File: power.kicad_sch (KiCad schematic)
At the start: 10 parts, among them J5 JST_PH_B2B, U2 MCP73831-2-OT, U3 AP1117-33

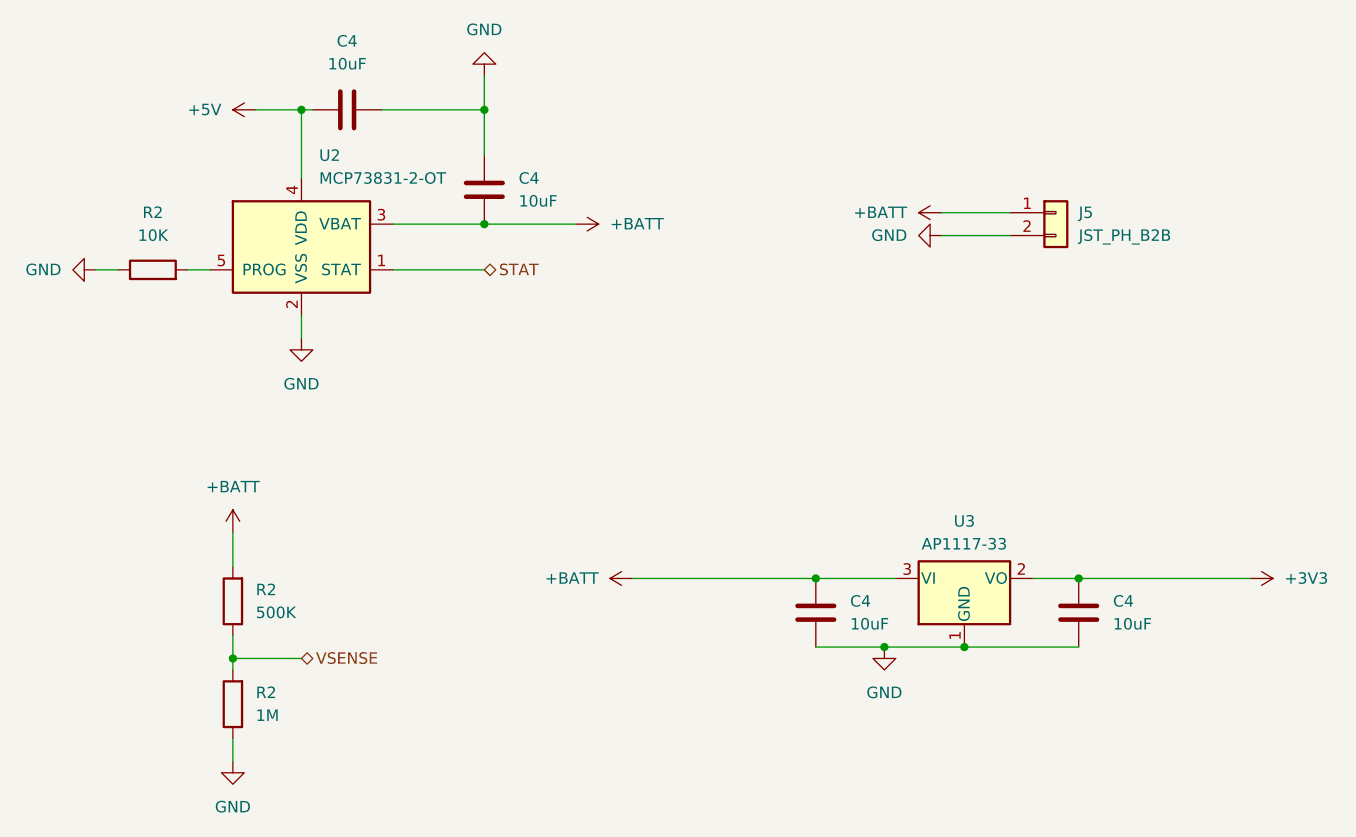
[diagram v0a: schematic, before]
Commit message: Removed audio, more routing
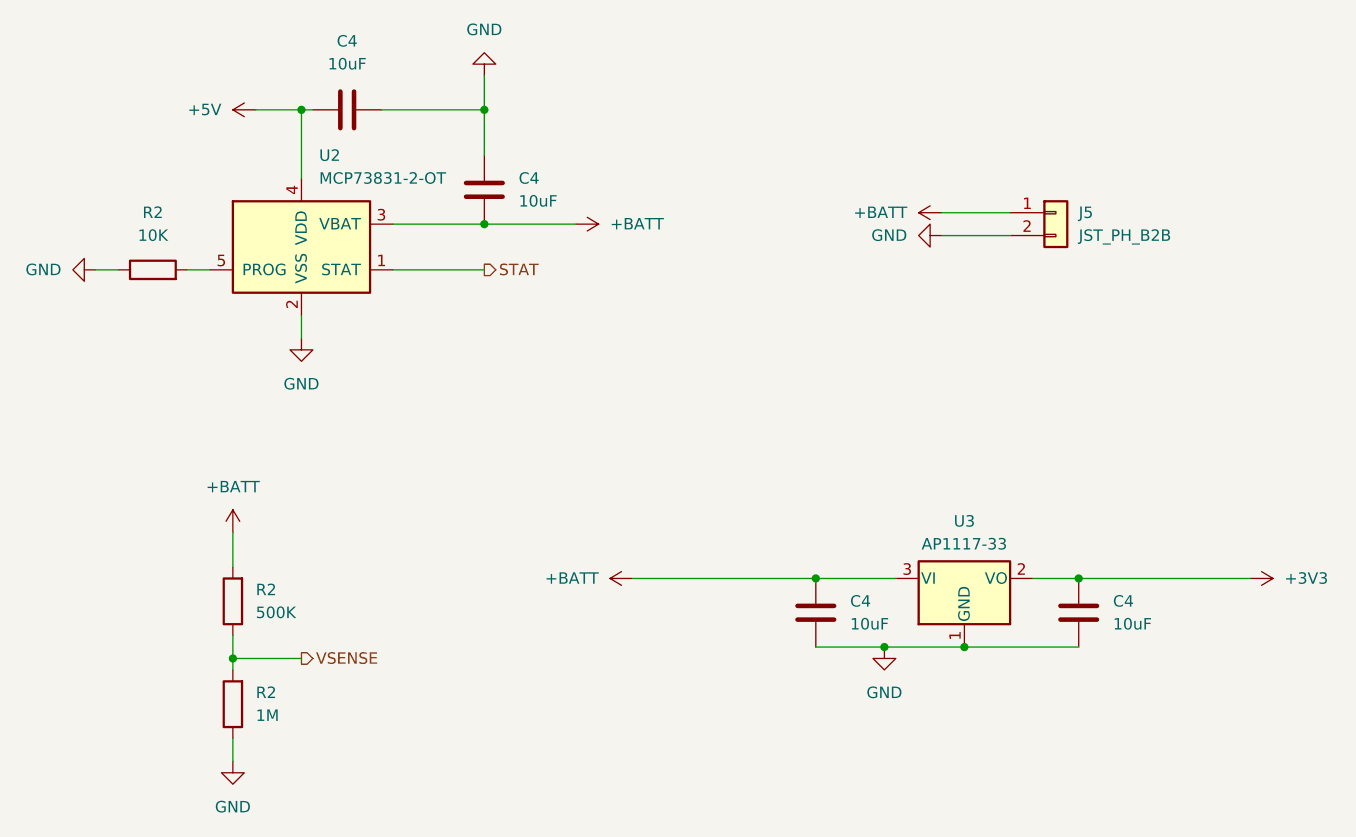
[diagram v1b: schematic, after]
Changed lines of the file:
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@@
     (stroke (width 0) (type default))
   )
-  (hierarchical_label "STAT" (shape bidirectional) (at 86.36 83.82 0) (fields_autoplaced)
+  (hierarchical_label "STAT" (shape output) (at 86.36 83.82 0) (fields_autoplaced)
     (effects (font (size 1.27 1.27)) (justify left))
   )
-  (hierarchical_label "VSENSE" (shape bidirectional) (at 66.04 127 0) (fields_autoplaced)
+  (hierarchical_label "VSENSE" (shape output) (at 66.04 127 0) (fields_autoplaced)
     (effects (font (size 1.27 1.27)) (justify left))
   )

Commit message: Field updates, generating fab files
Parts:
- removed U3: AP1117-33, Package_TO_SOT_SMD:SOT-223-3_TabPin2, symbol Regulator_Linear:AP1117-33
- added U3: HT7533-1, Package_TO_SOT_SMD:SOT-89-3, symbol Regulator_Linear:HT75xx-1-SOT89
- C4: value 10uF -> 10uF 20%; JLCPCB Part # (none) -> C315248
- J5: JLCPCB Part # (none) -> C131337
- R2: value 500K -> 510K 1%; JLCPCB Part # (none) -> C2909365
- R2: value 10K -> 10K 5%; JLCPCB Part # (none) -> C2906885
- R2: value 1M -> 1M 1%; JLCPCB Part # (none) -> C2906900
- U2: JLCPCB Part # (none) -> C424093
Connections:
- net +3V3: now also U3.3 (VOUT)
- net +BATT: now also U3.2 (VIN)
- net GND: now also U3.1 (GND)
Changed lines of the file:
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@@
   (junction (at 123.19 118.11) (diameter 0) (color 0 0 0 0)
   )
+  (junction (at 66.04 66.04) (diameter 0) (color 0 0 0 0)
+  )
+  (junction (at 152.4 118.11) (diameter 0) (color 0 0 0 0)
+  )
+  (junction (at 130.81 125.73) (diameter 0) (color 0 0 0 0)
+  )
+  (junction (at 58.42 127) (diameter 0) (color 0 0 0 0)
+  )
   (junction (at 139.7 125.73) (diameter 0) (color 0 0 0 0)
   )
-  (junction (at 66.04 66.04) (diameter 0) (color 0 0 0 0)
-  )
-  (junction (at 152.4 118.11) (diameter 0) (color 0 0 0 0)
-  )
-  (junction (at 130.81 125.73) (diameter 0) (color 0 0 0 0)
-  )
-  (junction (at 58.42 127) (diameter 0) (color 0 0 0 0)
-  )
   (junction (at 86.36 66.04) (diameter 0) (color 0 0 0 0)
   )
@@
     (stroke (width 0) (type default))
   )
+  (wire (pts (xy 139.7 125.73) (xy 152.4 125.73))
+    (stroke (width 0) (type default))
+  )
   (wire (pts (xy 102.87 118.11) (xy 123.19 118.11))
     (stroke (width 0) (type default))
@@
   )
   (wire (pts (xy 58.42 127) (xy 66.04 127))
-    (stroke (width 0) (type default))
-  )
-  (wire (pts (xy 139.7 125.73) (xy 152.4 125.73))
     (stroke (width 0) (type default))
   )
@@
       (effects (font (size 1.27 1.27)) (justify right))
     )
-    (property "Value" "500K" (at 60.96 121.92 0)
+    (property "Value" "510K 1%" (at 60.96 121.92 0)
       (effects (font (size 1.27 1.27)) (justify right))
     )
@@
       (effects (font (size 1.27 1.27)) hide)
     )
-    (property "Datasheet" "~" (at 58.42 120.65 0)
+    (property "Datasheet" "https://www.lcsc.com/product-detail/Chip-Resistor-Surface-Mount_FOJAN-FRC0402F5103TS_C2909365.html" (at 58.42 120.65 0)
+      (effects (font (size 1.27 1.27)) hide)
+    )
+    (property "JLCPCB Part #" "C2909365" (at 58.42 120.65 0)
       (effects (font (size 1.27 1.27)) hide)
     )
@@
       (effects (font (size 1.27 1.27)))
     )
-    (property "Value" "10uF" (at 71.12 60.96 90)
+    (property "Value" "10uF 20%" (at 71.12 60.96 90)
       (effects (font (size 1.27 1.27)))
     )
@@
       (effects (font (size 1.27 1.27)) hide)
     )
-    (property "Datasheet" "~" (at 71.12 66.04 0)
+    (property "Datasheet" "https://www.lcsc.com/product-detail/Multilayer-Ceramic-Capacitors-MLCC-SMD-SMT_Samsung-Electro-Mechanics-CL05A106MP5NUNC_C315248.html" (at 71.12 66.04 0)
+      (effects (font (size 1.27 1.27)) hide)
+    )
+    (property "JLCPCB Part #" "C315248" (at 71.12 66.04 0)
       (effects (font (size 1.27 1.27)) hide)
     )
@@
       (effects (font (size 1.27 1.27)) hide)
     )
-    (property "Datasheet" "~" (at 149.86 77.47 0)
+    (property "Datasheet" "https://www.lcsc.com/product-detail/Wire-To-Board-Wire-To-Wire-Connector_span-style-background-color-ff0-JST-span-Sales-America-B2B-PH-K-S-LF-SN_C131337.html" (at 149.86 77.47 0)
+      (effects (font (size 1.27 1.27)) hide)
+    )
+    (property "JLCPCB Part #" "C131337" (at 149.86 77.47 0)
       (effects (font (size 1.27 1.27)) hide)
     )
@@
       (effects (font (size 1.27 1.27)))
     )
-    (property "Value" "10K" (at 49.53 80.01 90)
+    (property "Value" "10K 5%" (at 49.53 80.01 90)
       (effects (font (size 1.27 1.27)))
     )
@@
       (effects (font (size 1.27 1.27)) hide)
     )
-    (property "Datasheet" "~" (at 49.53 83.82 0)
+    (property "Datasheet" "https://www.lcsc.com/product-detail/Chip-Resistor-Surface-Mount_FOJAN-FRC0402J103-TS_C2906885.html" (at 49.53 83.82 0)
+      (effects (font (size 1.27 1.27)) hide)
+    )
+    (property "JLCPCB Part #" "C2906885" (at 49.53 83.82 0)
       (effects (font (size 1.27 1.27)) hide)
     )
@@
     )
     (property "Datasheet" "http://ww1.microchip.com/downloads/en/DeviceDoc/20001984g.pdf" (at 62.23 82.55 0)
+      (effects (font (size 1.27 1.27)) hide)
+    )
+    (property "JLCPCB Part #" "C424093" (at 66.04 81.28 0)
       (effects (font (size 1.27 1.27)) hide)
     )
@@
       (effects (font (size 1.27 1.27)) (justify right))
     )
-    (property "Value" "10uF" (at 90.17 76.2 0)
+    (property "Value" "10uF 20%" (at 90.17 76.2 0)
       (effects (font (size 1.27 1.27)) (justify right))
     )
@@
       (effects (font (size 1.27 1.27)) hide)
     )
-    (property "Datasheet" "~" (at 86.36 74.93 0)
+    (property "Datasheet" "https://www.lcsc.com/product-detail/Multilayer-Ceramic-Capacitors-MLCC-SMD-SMT_Samsung-Electro-Mechanics-CL05A106MP5NUNC_C315248.html" (at 86.36 74.93 0)
+      (effects (font (size 1.27 1.27)) hide)
+    )
+    (property "JLCPCB Part #" "C315248" (at 86.36 74.93 0)
       (effects (font (size 1.27 1.27)) hide)
     )
@@
       (effects (font (size 1.27 1.27)) (justify right))
     )
-    (property "Value" "1M" (at 60.96 133.35 0)
+    (property "Value" "1M 1%" (at 60.96 133.35 0)
       (effects (font (size 1.27 1.27)) (justify right))
     )
@@
       (effects (font (size 1.27 1.27)) hide)
     )
-    (property "Datasheet" "~" (at 58.42 132.08 0)
+    (property "Datasheet" "https://www.lcsc.com/product-detail/Chip-Resistor-Surface-Mount_FOJAN-FRC0402J105-TS_C2906900.html" (at 58.42 132.08 0)
+      (effects (font (size 1.27 1.27)) hide)
+    )
+    (property "JLCPCB Part #" "C2906900" (at 58.42 132.08 0)
       (effects (font (size 1.27 1.27)) hide)
     )
@@
       (effects (font (size 1.27 1.27)) (justify right))
     )
-    (property "Value" "10uF" (at 127 123.19 0)
+    (property "Value" "10uF 20%" (at 127 123.19 0)
       (effects (font (size 1.27 1.27)) (justify right))
     )
@@
       (effects (font (size 1.27 1.27)) hide)
     )
-    (property "Datasheet" "~" (at 123.19 121.92 0)
+    (property "Datasheet" "https://www.lcsc.com/product-detail/Multilayer-Ceramic-Capacitors-MLCC-SMD-SMT_Samsung-Electro-Mechanics-CL05A106MP5NUNC_C315248.html" (at 123.19 121.92 0)
+      (effects (font (size 1.27 1.27)) hide)
+    )
+    (property "JLCPCB Part #" "C315248" (at 123.19 121.92 0)
       (effects (font (size 1.27 1.27)) hide)
     )
@@
     )
   )
+  (symbol (lib_id "Regulator_Linear:HT75xx-1-SOT89") (at 139.7 120.65 0) (unit 1)
+    (in_bom yes) (on_board yes) (dnp no) (fields_autoplaced)
+    (property "Reference" "U3" (at 139.7 110.49 0)
+      (effects (font (size 1.27 1.27)))
+    )
+    (property "Value" "HT7533-1" (at 139.7 113.03 0)
+      (effects (font (size 1.27 1.27)))
+    )
+    (property "Footprint" "Package_TO_SOT_SMD:SOT-89-3" (at 139.7 112.395 0)
+      (effects (font (size 1.27 1.27) italic) hide)
+    )
+    (property "Datasheet" "https://www.holtek.com/documents/10179/116711/HT75xx-1v250.pdf" (at 139.7 118.11 0)
+      (effects (font (size 1.27 1.27)) hide)
+    )
+    (property "JLCPCB Part #" "C14289" (at 139.7 120.65 0)
+      (effects (font (size 1.27 1.27)) hide)
+    )
+    (pin "1")
+    (pin "2")
+    (pin "3")
+    (instances
+      (project "reaction-trainer"
+        (path "/726cb70d-0185-4970-973b-037545fc3942/18baac07-1cb8-4cbd-b34a-df08336e3e3b"
+          (reference "U3") (unit 1)
+        )
+      )
+    )
+  )
   (symbol (lib_id "power:+BATT") (at 137.16 77.47 90) (unit 1)
     (in_bom yes) (on_board yes) (dnp no) (fields_autoplaced)
@@
     )
   )
-  (symbol (lib_id "Regulator_Linear:AP1117-33") (at 139.7 118.11 0) (unit 1)
-    (in_bom yes) (on_board yes) (dnp no) (fields_autoplaced)
-    (property "Reference" "U3" (at 139.7 111.76 0)
-      (effects (font (size 1.27 1.27)))
-    )
-    (property "Value" "AP1117-33" (at 139.7 114.3 0)
-      (effects (font (size 1.27 1.27)))
-    )
-    (property "Footprint" "Package_TO_SOT_SMD:SOT-223-3_TabPin2" (at 139.7 113.03 0)
-      (effects (font (size 1.27 1.27)) hide)
-    )
-    (property "Datasheet" "http://www.diodes.com/datasheets/AP1117.pdf" (at 142.24 124.46 0)
-      (effects (font (size 1.27 1.27)) hide)
-    )
-    (pin "1")
-    (pin "2")
-    (pin "3")
-    (instances
-      (project "reaction-trainer"
-        (path "/726cb70d-0185-4970-973b-037545fc3942/18baac07-1cb8-4cbd-b34a-df08336e3e3b"
-          (reference "U3") (unit 1)
-        )
-      )
-    )
-  )
   (symbol (lib_id "Device:C") (at 152.4 121.92 180) (unit 1)
     (in_bom yes) (on_board yes) (dnp no) (fields_autoplaced)
@@
       (effects (font (size 1.27 1.27)) (justify right))
     )
-    (property "Value" "10uF" (at 156.21 123.19 0)
+    (property "Value" "10uF 20%" (at 156.21 123.19 0)
       (effects (font (size 1.27 1.27)) (justify right))
     )
@@
       (effects (font (size 1.27 1.27)) hide)
     )
-    (property "Datasheet" "~" (at 152.4 121.92 0)
-      (effects (font (size 1.27 1.27)) hide)
-    )
+    (property "Datasheet" "https://www.lcsc.com/product-detail/Multilayer-Ceramic-Capacitors-MLCC-SMD-SMT_Samsung-Electro-Mechanics-CL05A106MP5NUNC_C315248.html" (at 152.4 121.92 0)
+      (effects (font (size 1.27 1.27)) hide)
+    )
+    (property "JLCPCB Part #" "C315248" (at 152.4 121.92 0)
+      (effects (font (size 1.27 1.27)) hide)
+    )

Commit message: Changed outline for DFM
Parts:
- C4: JLCPCB Part # C315248 -> (none); LCSC (none) -> C315248
- J5: JLCPCB Part # C131337 -> (none); LCSC (none) -> C131337
- R2: JLCPCB Part # C2909365 -> (none); LCSC (none) -> C2909365
- R2: JLCPCB Part # C2906885 -> (none); LCSC (none) -> C2906885
- R2: JLCPCB Part # C2906900 -> (none); LCSC (none) -> C2906900
- U2: JLCPCB Part # C424093 -> (none); LCSC (none) -> C424093
- U3: JLCPCB Part # C14289 -> (none); LCSC (none) -> C14289
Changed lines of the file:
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@@
       (effects (font (size 1.27 1.27)) hide)
     )
-    (property "JLCPCB Part #" "C2909365" (at 58.42 120.65 0)
+    (property "LCSC" "C2909365" (at 58.42 120.65 0)
       (effects (font (size 1.27 1.27)) hide)
     )
@@
       (effects (font (size 1.27 1.27)) hide)
     )
-    (property "JLCPCB Part #" "C315248" (at 71.12 66.04 0)
+    (property "LCSC" "C315248" (at 71.12 66.04 0)
       (effects (font (size 1.27 1.27)) hide)
     )
@@
       (effects (font (size 1.27 1.27)) hide)
     )
-    (property "JLCPCB Part #" "C131337" (at 149.86 77.47 0)
+    (property "LCSC" "C131337" (at 149.86 77.47 0)
       (effects (font (size 1.27 1.27)) hide)
     )
@@
       (effects (font (size 1.27 1.27)) hide)
     )
-    (property "JLCPCB Part #" "C2906885" (at 49.53 83.82 0)
+    (property "LCSC" "C2906885" (at 49.53 83.82 0)
       (effects (font (size 1.27 1.27)) hide)
     )
@@
       (effects (font (size 1.27 1.27)) hide)
     )
-    (property "JLCPCB Part #" "C424093" (at 66.04 81.28 0)
+    (property "LCSC" "C424093" (at 66.04 81.28 0)
       (effects (font (size 1.27 1.27)) hide)
     )
@@
       (effects (font (size 1.27 1.27)) hide)
     )
-    (property "JLCPCB Part #" "C315248" (at 86.36 74.93 0)
+    (property "LCSC" "C315248" (at 86.36 74.93 0)
       (effects (font (size 1.27 1.27)) hide)
     )
@@
       (effects (font (size 1.27 1.27)) hide)
     )
-    (property "JLCPCB Part #" "C2906900" (at 58.42 132.08 0)
+    (property "LCSC" "C2906900" (at 58.42 132.08 0)
       (effects (font (size 1.27 1.27)) hide)
     )
@@
       (effects (font (size 1.27 1.27)) hide)
     )
-    (property "JLCPCB Part #" "C315248" (at 123.19 121.92 0)
+    (property "LCSC" "C315248" (at 123.19 121.92 0)
       (effects (font (size 1.27 1.27)) hide)
     )
@@
       (effects (font (size 1.27 1.27)) hide)
     )
-    (property "JLCPCB Part #" "C14289" (at 139.7 120.65 0)
+    (property "LCSC" "C14289" (at 139.7 120.65 0)
       (effects (font (size 1.27 1.27)) hide)
     )
@@
       (effects (font (size 1.27 1.27)) hide)
     )
-    (property "JLCPCB Part #" "C315248" (at 152.4 121.92 0)
-      (effects (font (size 1.27 1.27)) hide)
-    )
+    (property "LCSC" "C315248" (at 152.4 121.92 0)
+      (effects (font (size 1.27 1.27)) hide)
+    )
